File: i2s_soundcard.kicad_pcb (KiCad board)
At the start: 4 copper layers, 83.1 x 50 mm, 19 parts, among them J1 Conn_01x08, J2 Conn_01x06, J3 Conn_01x05, J4 Conn_01x11, J5 Conn_01x04, U1 TLV320AIC3104IRHBT, U2 FSA2275UMX, U3 TPA2006D1DRBR, U4 FSA2275UMX, U5 TPA2006D1DRBR, U6 TLV7111830DSER

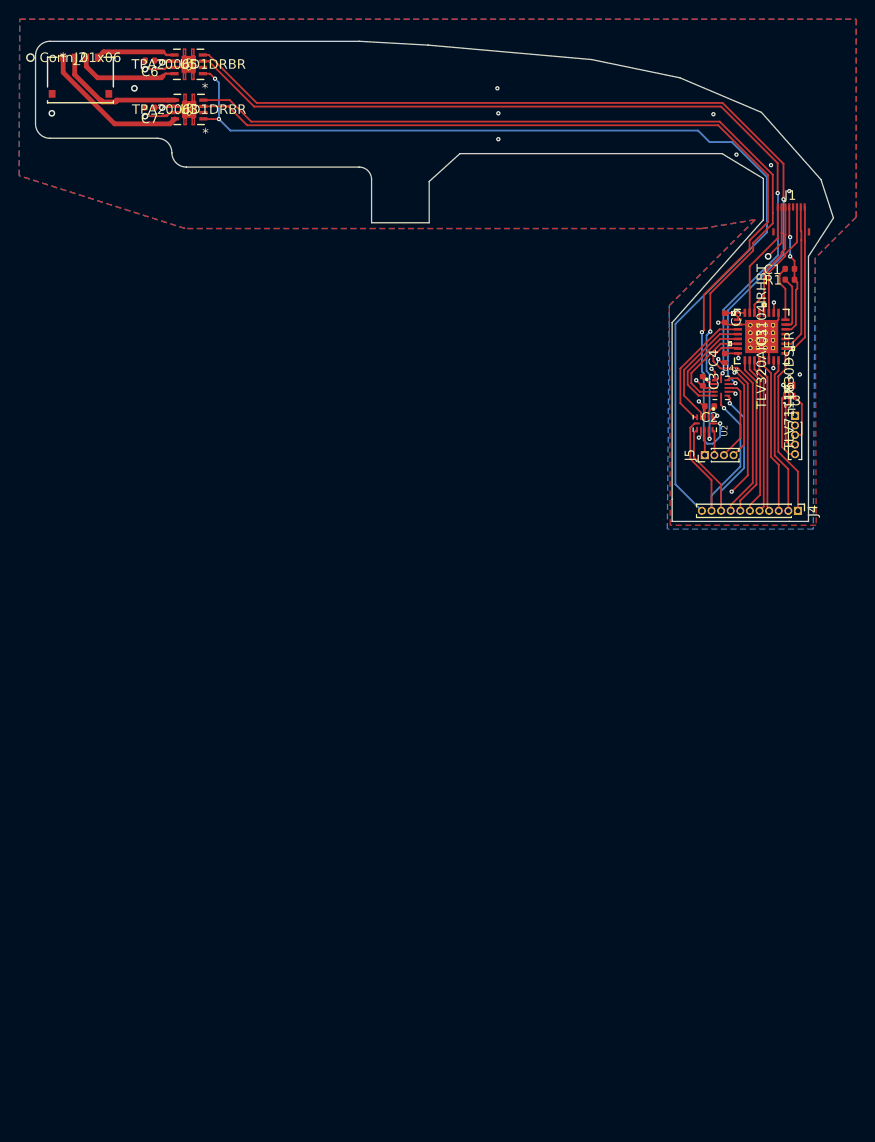
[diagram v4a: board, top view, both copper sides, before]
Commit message: Clean up silkscreen, add some silkscreen labels to pin headers.
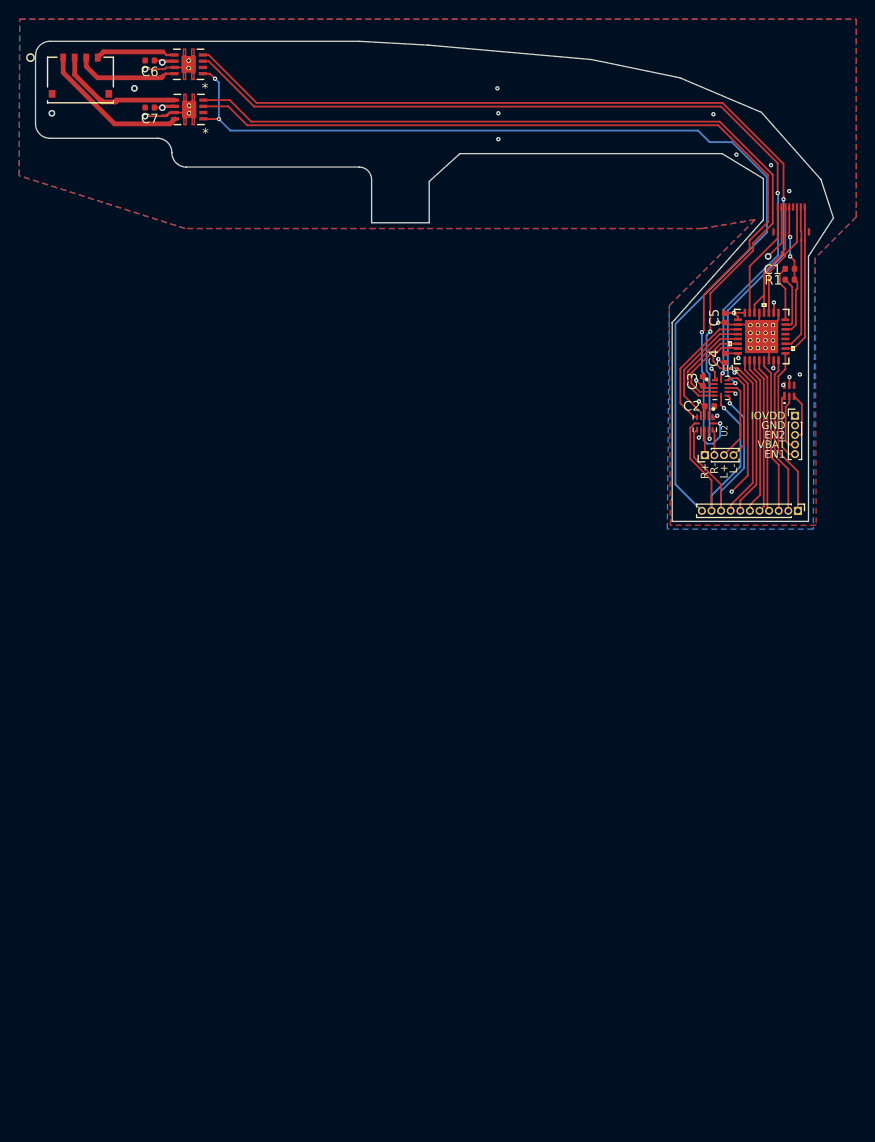
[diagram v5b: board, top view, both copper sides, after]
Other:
- board text added: "BCLK"
- board text added: "DIN"
- board text added: "DOUT"
- board text added: "EN1"
- board text added: "EN2"
- board text added: "GND"
- board text added: "IOVDD"
- board text added: "L+"
- board text added: "L-"
- board text added: "MCLK"
- board text added: "MUTE"
- board text added: "R+"
- board text added: "R-"
- board text added: "RST"
- board text added: "SCL"
- board text added: "SDA"
- board text added: "SEL"
- board text added: "VBAT"
- board text added: "WCLK"
- board text added: "~SD"
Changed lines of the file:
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@@
   (general
     (thickness 1)
-    (drawings 41)
+    (drawings 61)
     (tracks 424)
     (zones 0)
@@
   (page A4)
   (layers
-    (0 F.Cu signal)
-    (1 In1.Cu power)
-    (2 In2.Cu power)
-    (31 B.Cu signal)
-    (32 B.Adhes user)
-    (33 F.Adhes user)
-    (34 B.Paste user)
-    (35 F.Paste user hide)
+    (0 F.Cu signal hide)
+    (1 In1.Cu power hide)
+    (2 In2.Cu power hide)
+    (31 B.Cu signal hide)
+    (32 B.Adhes user hide)
+    (33 F.Adhes user hide)
+    (34 B.Paste user hide)
+    (35 F.Paste user)
     (36 B.SilkS user hide)
-    (37 F.SilkS user hide)
-    (38 B.Mask user hide)
+    (37 F.SilkS user)
+    (38 B.Mask user)
     (39 F.Mask user hide)
     (40 Dwgs.User user hide)
     (41 Cmts.User user hide)
-    (42 Eco1.User user)
-    (43 Eco2.User user)
+    (42 Eco1.User user hide)
+    (43 Eco2.User user hide)
     (44 Edge.Cuts user)
-    (45 Margin user)
-    (46 B.CrtYd user)
-    (47 F.CrtYd user)
-    (48 B.Fab user)
+    (45 Margin user hide)
+    (46 B.CrtYd user hide)
+    (47 F.CrtYd user hide)
+    (48 B.Fab user hide)
     (49 F.Fab user hide)
   )
@@
     (descr "Through hole straight pin header, 1x11, 1.00mm pitch, single row")
     (tags "Through hole pin header THT 1x11 1.00mm single row")
-    (fp_text reference J4 (at 0 -1.56 90) (layer F.SilkS)
+    (fp_text reference J4 (at 0 -1.56 90) (layer F.SilkS) hide
       (effects (font (size 1 1) (thickness 0.15)))
     )
@@
     (descr "Through hole straight pin header, 1x04, 1.00mm pitch, single row")
     (tags "Through hole pin header THT 1x04 1.00mm single row")
-    (fp_text reference J5 (at 0 -1.56 90) (layer F.SilkS)
+    (fp_text reference J5 (at 0 -1.56 90) (layer F.SilkS) hide
       (effects (font (size 1 1) (thickness 0.15)))
     )
@@
     (descr "Through hole straight pin header, 1x05, 1.00mm pitch, single row")
     (tags "Through hole pin header THT 1x05 1.00mm single row")
-    (fp_text reference J3 (at 0 -1.56) (layer F.SilkS)
+    (fp_text reference J3 (at 2.55 0.01) (layer F.SilkS) hide
       (effects (font (size 1 1) (thickness 0.15)))
     )
@@
   (module footprints:TPA2006D1DRBR (layer F.Cu)
     (at 103.8 65.4 180)
-    (fp_text reference U3 (at 0 0) (layer F.SilkS)
-      (effects (font (size 1 1) (thickness 0.15)))
-    )
-    (fp_text value TPA2006D1DRBR (at 0 0) (layer F.SilkS)
+    (fp_text reference U3 (at 0 0) (layer F.SilkS) hide
+      (effects (font (size 1 1) (thickness 0.15)))
+    )
+    (fp_text value TPA2006D1DRBR (at 0 0) (layer F.SilkS) hide
       (effects (font (size 1 1) (thickness 0.15)))
     )
@@
   (module footprints:TPA2006D1DRBR (layer F.Cu)
     (at 103.75 60.7 180)
-    (fp_text reference U5 (at 0 0) (layer F.SilkS)
-      (effects (font (size 1 1) (thickness 0.15)))
-    )
-    (fp_text value TPA2006D1DRBR (at 0 0) (layer F.SilkS)
+    (fp_text reference U5 (at 0 0) (layer F.SilkS) hide
+      (effects (font (size 1 1) (thickness 0.15)))
+    )
+    (fp_text value TPA2006D1DRBR (at 0 0) (layer F.SilkS) hide
       (effects (font (size 1 1) (thickness 0.15)))
     )
@@
   (module footprints:TLV7111830DSER (layer F.Cu)
     (at 166.3 94.7 90)
-    (fp_text reference U6 (at 0 0 90) (layer F.SilkS)
-      (effects (font (size 1 1) (thickness 0.15)))
-    )
-    (fp_text value TLV7111830DSER (at 0 0 90) (layer F.SilkS)
+    (fp_text reference U6 (at 0.04 0.03 90) (layer F.SilkS) hide
+      (effects (font (size 1 1) (thickness 0.15)))
+    )
+    (fp_text value TLV7111830DSER (at 0 0 90) (layer F.SilkS) hide
       (effects (font (size 1 1) (thickness 0.15)))
     )
@@
       (effects (font (size 1 1) (thickness 0.15)))
     )
-    (fp_text user * (at 0 0 90) (layer F.SilkS)
+    (fp_text user * (at 0 0 90) (layer F.SilkS) hide
       (effects (font (size 1 1) (thickness 0.15)))
     )
@@
     (tags capacitor)
     (attr smd)
-    (fp_text reference C5 (at 0 -1.17 90) (layer F.SilkS)
+    (fp_text reference C5 (at -0.02 1.12 90) (layer F.SilkS)
       (effects (font (size 1 1) (thickness 0.15)))
     )
@@
   (module footprints:TLV320AIC3104IRHBT (layer F.Cu)
     (at 163.425 89.05 90)
-    (fp_text reference U1 (at 0 0 90) (layer F.SilkS)
-      (effects (font (size 1 1) (thickness 0.15)))
-    )
-    (fp_text value TLV320AIC3104IRHBT (at 0 0 90) (layer F.SilkS)
+    (fp_text reference U1 (at 0 0 90) (layer F.SilkS) hide
+      (effects (font (size 1 1) (thickness 0.15)))
+    )
+    (fp_text value TLV320AIC3104IRHBT (at 0 0 90) (layer F.SilkS) hide
       (effects (font (size 1 1) (thickness 0.15)))
     )
@@
   (module footprints:78171-0004 (layer F.Cu)
     (at 90.68 60)
-    (fp_text reference J2 (at 1.8 0) (layer F.SilkS)
-      (effects (font (size 1 1) (thickness 0.15)))
-    )
-    (fp_text value Conn_01x06 (at 1.8 0) (layer F.SilkS)
+    (fp_text reference J2 (at 1.8 0) (layer F.SilkS) hide
+      (effects (font (size 1 1) (thickness 0.15)))
+    )
+    (fp_text value Conn_01x06 (at 1.8 0) (layer F.SilkS) hide
       (effects (font (size 1 1) (thickness 0.15)))
     )
@@
       (effects (font (size 1 1) (thickness 0.15)))
     )
-    (fp_text user * (at 0 0) (layer F.SilkS)
+    (fp_text user * (at -0.01 -0.57) (layer F.SilkS) hide
       (effects (font (size 1 1) (thickness 0.15)))
     )
@@
   (module footprints:FF18-8A-R11AD-B-3H (layer F.Cu)
     (at 166.5 76.85 180)
-    (fp_text reference J1 (at 0.1 2.5) (layer F.SilkS)
+    (fp_text reference J1 (at 0.1 2.5) (layer F.SilkS) hide
       (effects (font (size 1 1) (thickness 0.15)))
     )
@@
     (tags capacitor)
     (attr smd)
-    (fp_text reference C3 (at 0 -1.17 90) (layer F.SilkS)
+    (fp_text reference C3 (at 0.01 1.09 90) (layer F.SilkS)
       (effects (font (size 1 1) (thickness 0.15)))
     )
@@
     (tags capacitor)
     (attr smd)
-    (fp_text reference C2 (at 0 -1.17) (layer F.SilkS)
+    (fp_text reference C2 (at 1.85 0) (layer F.SilkS)
       (effects (font (size 1 1) (thickness 0.15)))
     )
@@
       (rotate (xyz 0 0 0))
     )
+  )
+  (gr_text EN1 (at 165.9 101.3) (layer F.SilkS)
+    (effects (font (size 0.8 0.8) (thickness 0.15)) (justify right))
+  )
+  (gr_text VBAT (at 165.9 100.3) (layer F.SilkS)
+    (effects (font (size 0.8 0.8) (thickness 0.15)) (justify right))
+  )
+  (gr_text EN2 (at 165.9 99.3) (layer F.SilkS)
+    (effects (font (size 0.8 0.8) (thickness 0.15)) (justify right))
+  )
+  (gr_text GND (at 165.9 98.3) (layer F.SilkS)
+    (effects (font (size 0.8 0.8) (thickness 0.15)) (justify right))
+  )
+  (gr_text IOVDD (at 165.9 97.3) (layer F.SilkS)
+    (effects (font (size 0.8 0.8) (thickness 0.15)) (justify right))
+  )
+  (gr_text SCL (at 166.2 106.5 -90) (layer B.SilkS)
+    (effects (font (size 0.8 0.8) (thickness 0.15)) (justify left mirror))
+  )
+  (gr_text SDA (at 167.2 106.5 -90) (layer B.SilkS)
+    (effects (font (size 0.8 0.8) (thickness 0.15)) (justify left mirror))
+  )
+  (gr_text DOUT (at 165.2 106.5 -90) (layer B.SilkS)
+    (effects (font (size 0.8 0.8) (thickness 0.15)) (justify left mirror))
+  )
+  (gr_text DIN (at 164.2 106.5 -90) (layer B.SilkS)
+    (effects (font (size 0.8 0.8) (thickness 0.15)) (justify left mirror))
+  )
+  (gr_text WCLK (at 163.2 106.5 -90) (layer B.SilkS)
+    (effects (font (size 0.8 0.8) (thickness 0.15)) (justify left mirror))
+  )
+  (gr_text BCLK (at 162.2 106.5 -90) (layer B.SilkS)
+    (effects (font (size 0.8 0.8) (thickness 0.15)) (justify left mirror))
+  )
+  (gr_text MCLK (at 161.2 106.5 -90) (layer B.SilkS)
+    (effects (font (size 0.8 0.8) (thickness 0.15)) (justify left mirror))
+  )
+  (gr_text RST (at 160.2 106.5 -90) (layer B.SilkS)
+    (effects (font (size 0.8 0.8) (thickness 0.15)) (justify left mirror))
+  )
+  (gr_text MUTE (at 159.2 106.5 -90) (layer B.SilkS)
+    (effects (font (size 0.8 0.8) (thickness 0.15)) (justify left mirror))
+  )
+  (gr_text SEL (at 158.2 106.5 -90) (layer B.SilkS)
+    (effects (font (size 0.8 0.8) (thickness 0.15)) (justify left mirror))
+  )
+  (gr_text ~SD (at 157.2 106.5 -90) (layer B.SilkS)
+    (effects (font (size 0.8 0.8) (thickness 0.15)) (justify left mirror))
+  )
+  (gr_text L- (at 160.5 102.3 90) (layer F.SilkS)
+    (effects (font (size 0.8 0.8) (thickness 0.15)) (justify right))
+  )
+  (gr_text L+ (at 159.5 102.3 90) (layer F.SilkS)
+    (effects (font (size 0.8 0.8) (thickness 0.15)) (justify right))
+  )
+  (gr_text R- (at 158.5 102.2 90) (layer F.SilkS)
+    (effects (font (size 0.8 0.8) (thickness 0.15)) (justify right))
+  )
+  (gr_text R+ (at 157.5 102.2 90) (layer F.SilkS)
+    (effects (font (size 0.8 0.8) (thickness 0.15)) (justify right))
   )
   (gr_poly (pts (xy 154.9 62.1) (xy 163.4 65.7) (xy 169.6 72.7) (xy 170.9 76.7) (xy 168.3 80.7) (xy 167.7 80.8) (xy 166.3 74.9) (xy 161.6 69.1) (xy 153.8 65.9) (xy 145.6 64.2) (xy 122.7 62.6) (xy 122.8 58.4) (xy 128.7 58.7) (xy 145.7 60.2)) (layer B.Mask) (width 0.1))
@@
   (segment (start 159.814685 87.799685) (end 159.6 87.585) (width 0.19) (layer F.Cu) (net 3))
   (segment (start 160.950001 87.799685) (end 159.814685 87.799685) (width 0.19) (layer F.Cu) (net 3))
-  (segment (start 164.175001 89.800001) (end 163.425 89.05) (width 0.19) (layer F.Cu) (net 3))
+  (segment (start 164.175001 89.800001) (end 163.425 89.05) (width 0.19) (layer F.Cu) (net 3) (status 1000000))
   (segment (start 164.175001 91.524999) (end 164.175001 89.800001) (width 0.19) (layer F.Cu) (net 3))
   (segment (start 165.174999 87.300001) (end 163.425 89.05) (width 0.19) (layer F.Cu) (net 3))

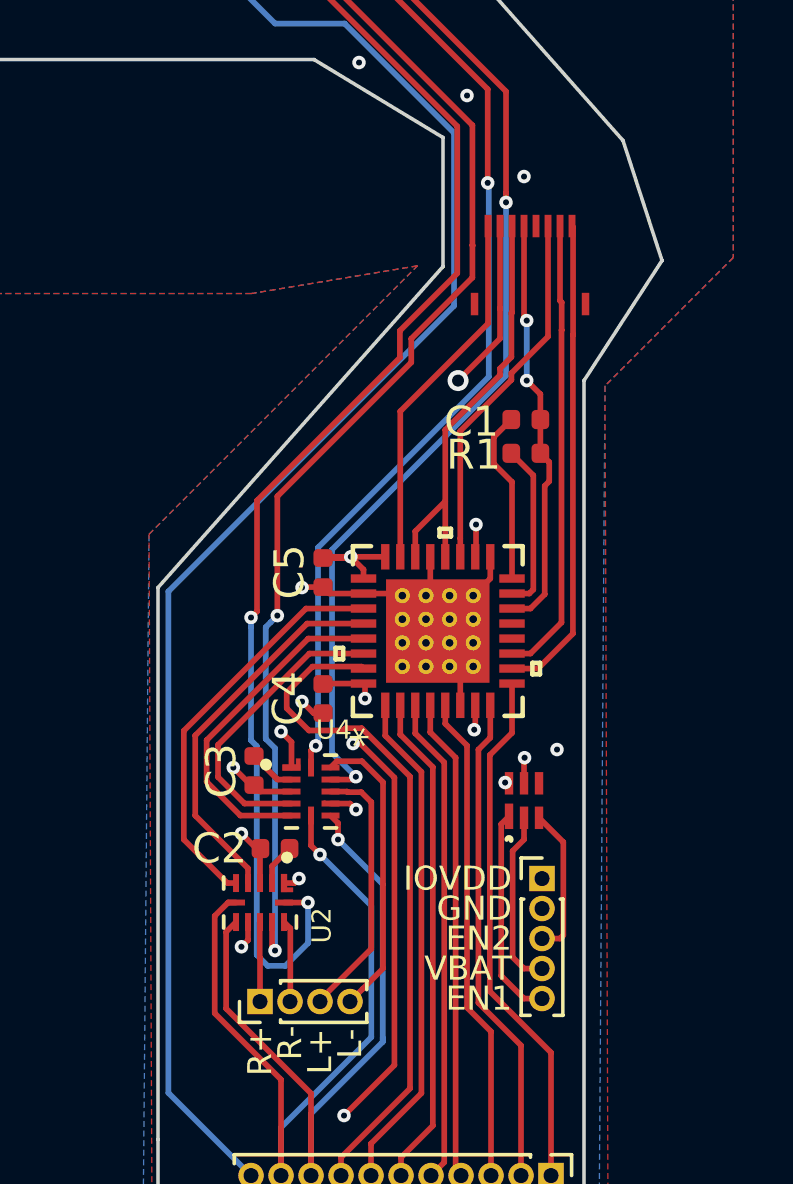
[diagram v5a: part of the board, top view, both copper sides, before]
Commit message: Add TVS diodes on all the headphone port pins
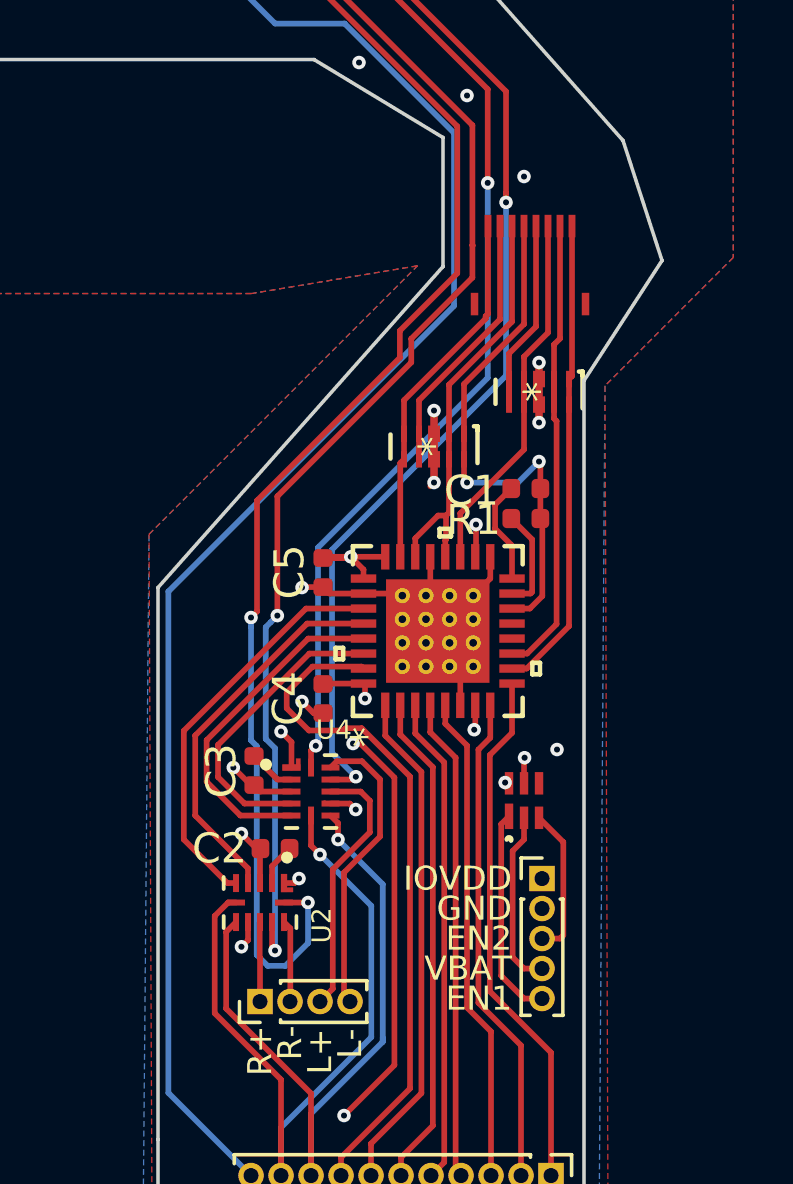
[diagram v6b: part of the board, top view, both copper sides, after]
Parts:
- added U7: TPD4E02B04DQAR, footprints:TPD4E02B04DQAR, F.Cu at (166.8, 81.1)
- added U8: TPD4E02B04DQAR, footprints:TPD4E02B04DQAR, F.Cu at (163.3, 82.9)
- moved C1 2.30 mm to (166.4, 84.3)
- moved R1 2.17 mm to (166.4, 85.3)
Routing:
- net /ring2: track 0.00 -> 7.17 mm
- net GND: track 45.8 -> 50.4 mm, vias 20 -> 24
- net /sleeve: track 14.0 -> 17.8 mm
- net Net-(J1-Pad7): track 5.73 -> 8.89 mm, vias 1 -> 0
- net Net-(C1-Pad1): track 5.98 -> 3.46 mm
- net Net-(R1-Pad2): track 5.61 -> 3.43 mm
- net /tip: track 12.2 -> 13.1 mm
- net /intmic-: track 15.3 -> 16.1 mm

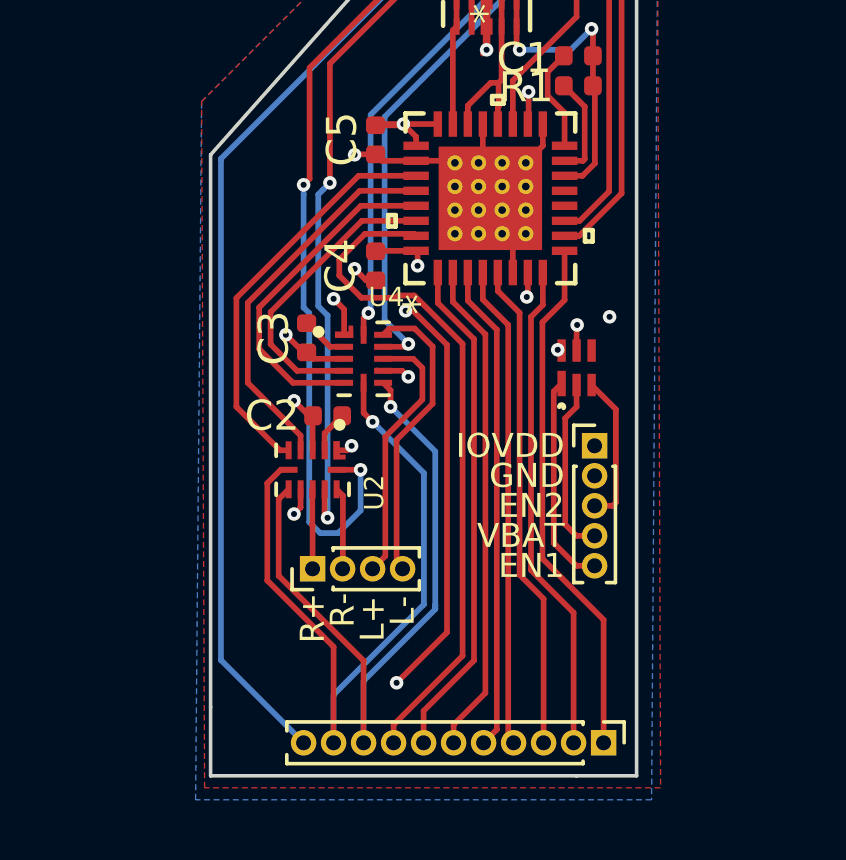
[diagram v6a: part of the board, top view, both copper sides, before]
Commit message: Rearrange pin headers to be on 1mm grid relative to each other
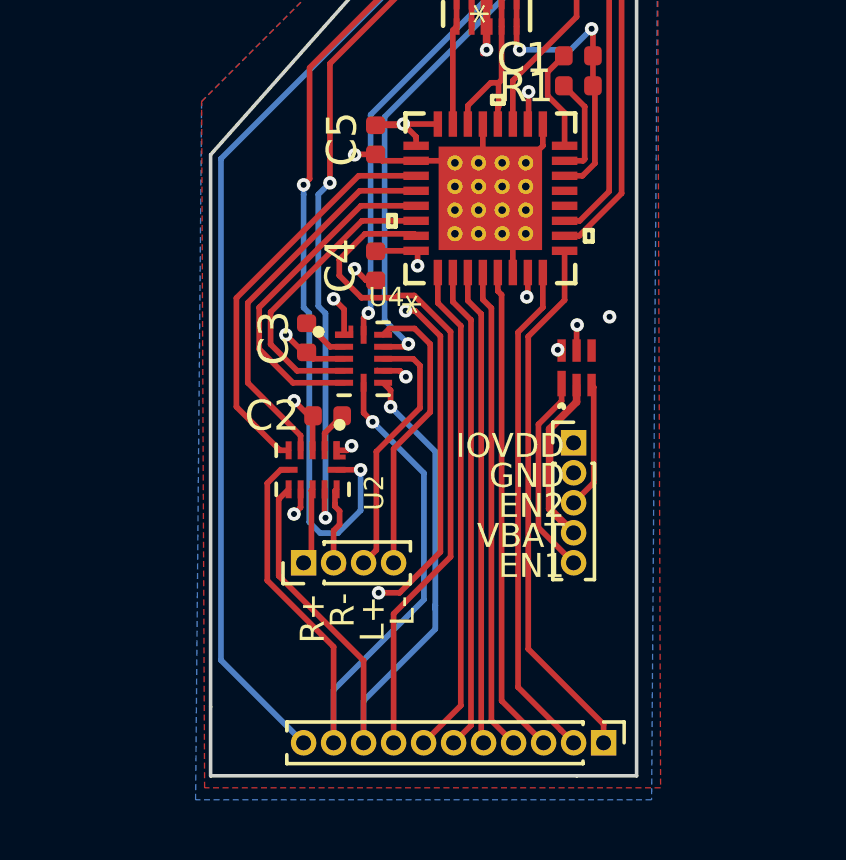
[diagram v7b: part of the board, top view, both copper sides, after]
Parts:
- moved J3 0.71 mm to (166.2, 97.2)
- moved J5 0.36 mm to (157.2, 101.2)
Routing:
- net GND: track 50.4 -> 47.8 mm
- net /vbat: track 27.0 -> 25.9 mm
- net /en2: track 5.03 -> 4.26 mm
